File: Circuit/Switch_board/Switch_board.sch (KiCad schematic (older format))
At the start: 17 parts, among them J1 switch_mode, J2 switch, P1 XT30, Q1 BSS138, Q2 BSS138, U1 DRV5023

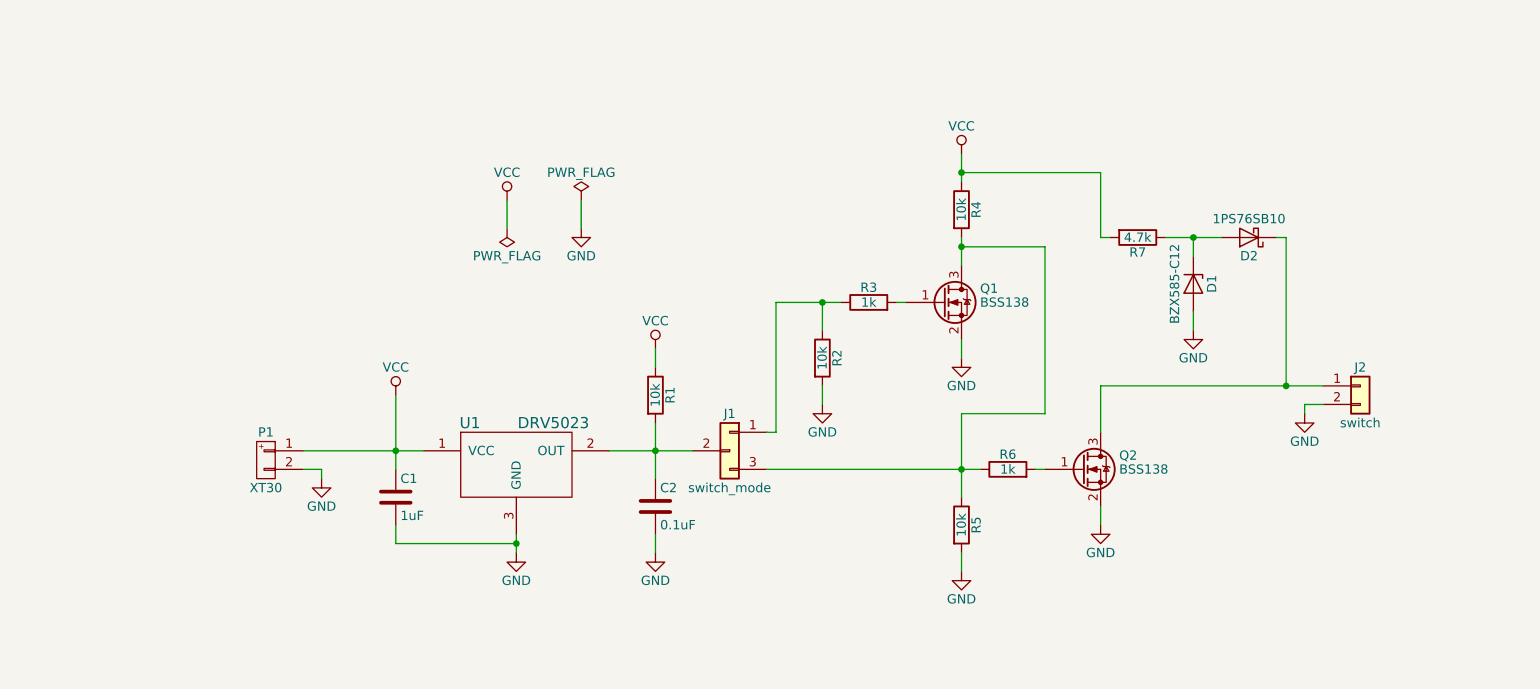
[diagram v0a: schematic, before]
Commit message: added status LED and change nMOSFET from BSS138 to 2N7002 in Switch_board
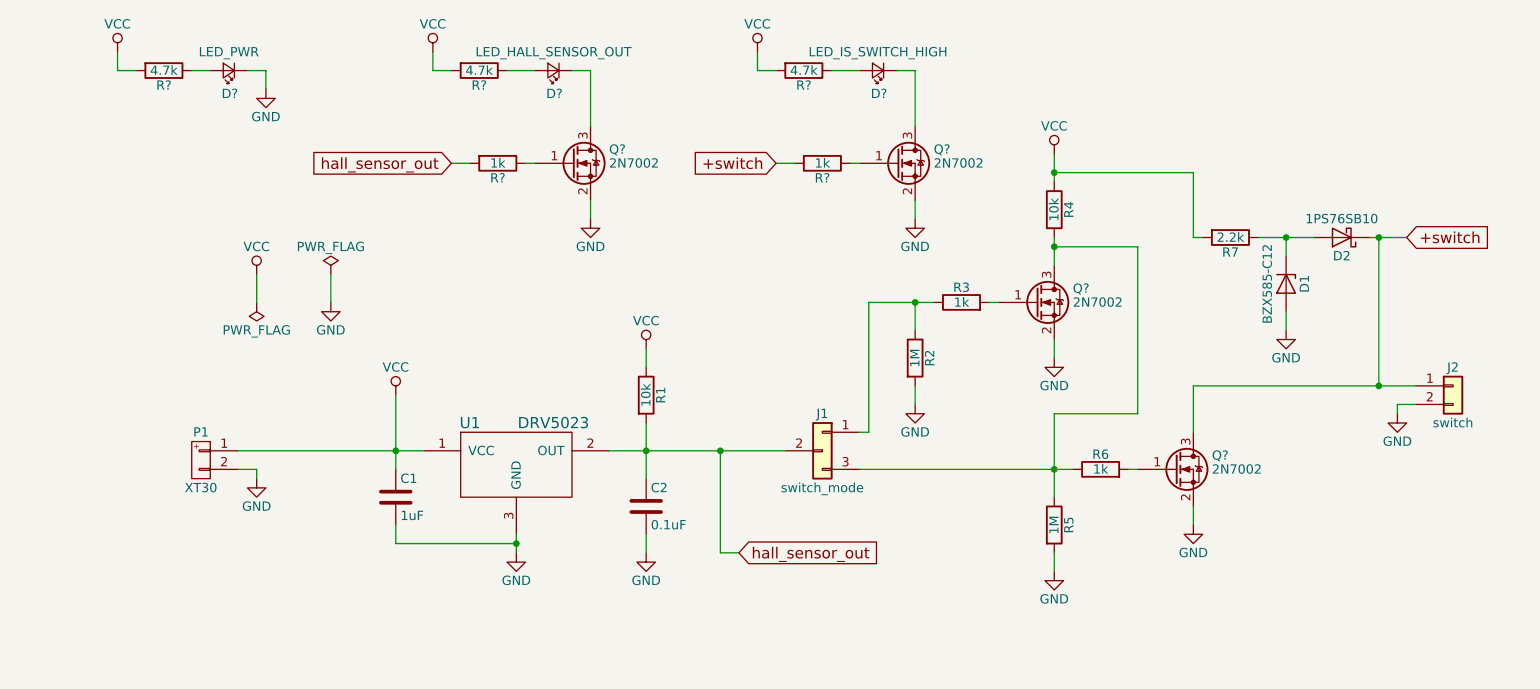
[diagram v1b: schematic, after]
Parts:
- removed Q1, Q2: BSS138, TO_SOT_Packages_SMD:SOT-23_Handsoldering, symbol BSS138
- added D?: LED_PWR, LEDs:LED_0603_HandSoldering, symbol LED_Small
- added D?: LED_HALL_SENSOR_OUT, LEDs:LED_0603_HandSoldering, symbol LED_Small
- added D?: LED_IS_SWITCH_HIGH, LEDs:LED_0603_HandSoldering, symbol LED_Small
- added Q? (x4): 2N7002, TO_SOT_Packages_SMD:SOT-23, symbol 2N7002
- added R? (x3): 4.7k, Resistors_SMD:R_0603_HandSoldering, symbol R
- added R? (x2): 1k, Resistors_SMD:R_0603_HandSoldering, symbol R
- R2, R5: value 10k -> 1M
- R7: value 4.7k -> 2.2k
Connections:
- net GND: now also D?.1 (K), Q?.2 (S), Q?.2 (S), Q?.2 (S), Q?.2 (S)
- net VCC: now also R?.2, R?.2, R?.2
- net hall_sensor_out: now reaches C2.1, J1.2 (Pin_2), R1.2, U1.2 (OUT)
- net hall_sensor_out: now also R?.2
- net at J1.3 (Pin_3), R4.2, R5.1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: now also Q?.3 (D)
- net +switch: now reaches D2.1 (K), J2.1 (Pin_1)
- net +switch: now also Q?.3 (D), R?.2
- net at R3.2: now also Q?.1 (G)
- net at R6.2: now also Q?.1 (G)
- new net: D?.2 (A), R?.1 (x3)
- new net: Q?.1 (G), R?.1 (x2)
- new net: D?.1 (K), Q?.3 (D) (x2)
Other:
- moved on the sheet: C2, D1, D2, J1, J2, P1, R1, R2, R3, R4, R5, R6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

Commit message: annoteted schematic and generated netlist of Switch_board
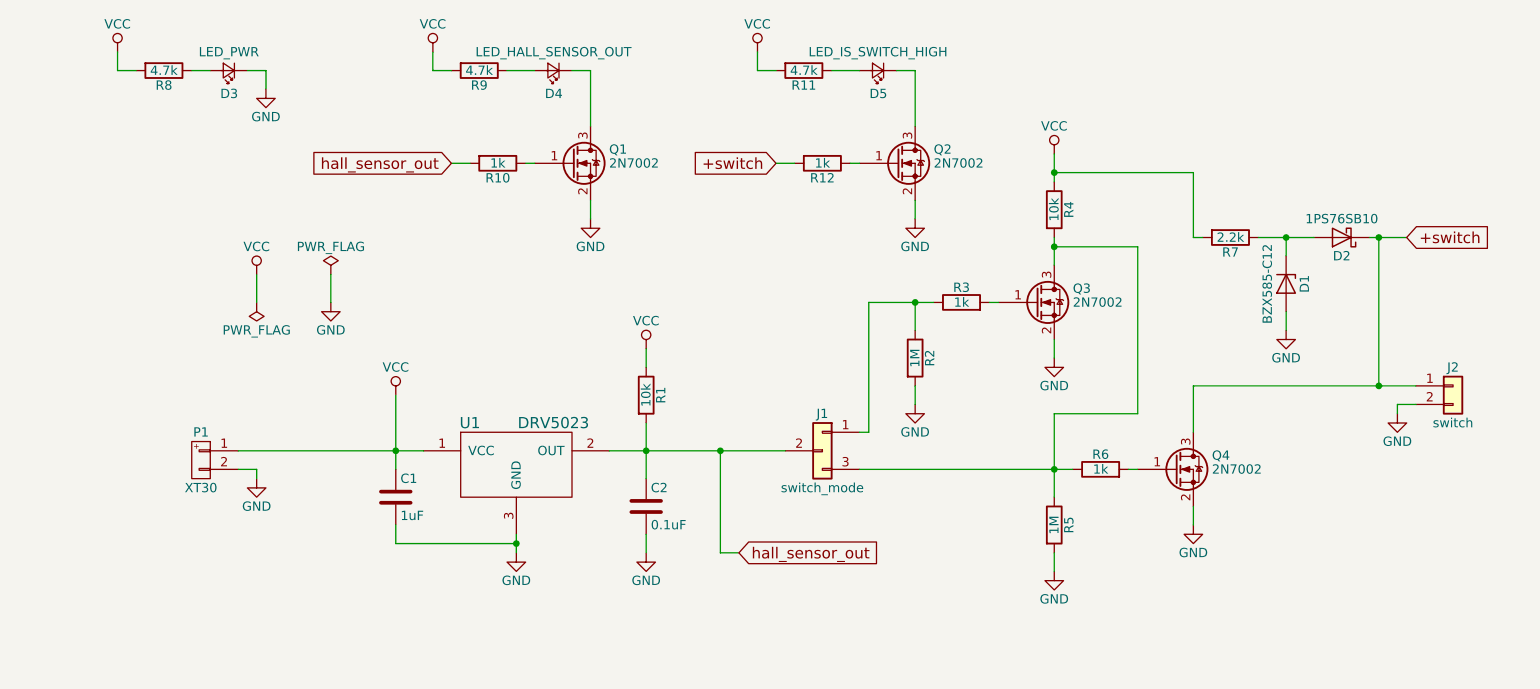
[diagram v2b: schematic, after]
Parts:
- gave numbers to parts that had none: 12
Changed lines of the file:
@@
 $EndComp
 $Comp
-L GND #PWR01
+L GND #PWR8
 U 1 1 5A826833
 P 3700 4750
-F 0 "#PWR01" H 3700 4500 50  0001 C CNN
+F 0 "#PWR8" H 3700 4500 50  0001 C CNN
 F 1 "GND" H 3700 4600 50  0000 C CNN
 F 2 "" H 3700 4750 50  0001 C CNN
@@
 $EndComp
 $Comp
-L GND #PWR02
+L GND #PWR3
 U 1 1 5A826918
 P 2300 4350
-F 0 "#PWR02" H 2300 4100 50  0001 C CNN
+F 0 "#PWR3" H 2300 4100 50  0001 C CNN
 F 1 "GND" H 2300 4200 50  0000 C CNN
 F 2 "" H 2300 4350 50  0001 C CNN
@@
 $EndComp
 $Comp
-L GND #PWR03
+L GND #PWR20
 U 1 1 5A829801
 P 8450 4000
-F 0 "#PWR03" H 8450 3750 50  0001 C CNN
+F 0 "#PWR20" H 8450 3750 50  0001 C CNN
 F 1 "GND" H 8450 3850 50  0000 C CNN
 F 2 "" H 8450 4000 50  0001 C CNN
@@
 $EndComp
 $Comp
-L GND #PWR04
+L GND #PWR14
 U 1 1 5A829CAE
 P 5850 3950
-F 0 "#PWR04" H 5850 3700 50  0001 C CNN
+F 0 "#PWR14" H 5850 3700 50  0001 C CNN
 F 1 "GND" H 5850 3800 50  0000 C CNN
 F 2 "" H 5850 3950 50  0001 C CNN
@@
 $EndComp
 $Comp
-L GND #PWR05
+L GND #PWR11
 U 1 1 5A883892
 P 4400 4750
-F 0 "#PWR05" H 4400 4500 50  0001 C CNN
+F 0 "#PWR11" H 4400 4500 50  0001 C CNN
 F 1 "GND" H 4400 4600 50  0000 C CNN
 F 2 "" H 4400 4750 50  0001 C CNN
@@
 $EndComp
 $Comp
-L GND #PWR06
+L GND #PWR16
 U 1 1 5A88921C
 P 6600 3700
-F 0 "#PWR06" H 6600 3450 50  0001 C CNN
+F 0 "#PWR16" H 6600 3450 50  0001 C CNN
 F 1 "GND" H 6600 3550 50  0000 C CNN
 F 2 "" H 6600 3700 50  0001 C CNN
@@
 $EndComp
 $Comp
-L VCC #PWR07
+L VCC #PWR6
 U 1 1 5A89DB47
 P 3050 3900
-F 0 "#PWR07" H 3050 3750 50  0001 C CNN
+F 0 "#PWR6" H 3050 3750 50  0001 C CNN
 F 1 "VCC" H 3050 4050 50  0000 C CNN
 F 2 "" H 3050 3900 50  0001 C CNN
@@
 $EndComp
 $Comp
-L GND #PWR08
+L GND #PWR19
 U 1 1 5A89F539
 P 7850 3550
-F 0 "#PWR08" H 7850 3300 50  0001 C CNN
+F 0 "#PWR19" H 7850 3300 50  0001 C CNN
 F 1 "GND" H 7850 3400 50  0000 C CNN
 F 2 "" H 7850 3550 50  0001 C CNN
@@
 $EndComp
 $Comp
-L GND #PWR09
+L GND #PWR17
 U 1 1 5A8DDCE5
 P 6600 4850
-F 0 "#PWR09" H 6600 4600 50  0001 C CNN
+F 0 "#PWR17" H 6600 4600 50  0001 C CNN
 F 1 "GND" H 6600 4700 50  0000 C CNN
 F 2 "" H 6600 4850 50  0001 C CNN
@@
 $EndComp
 $Comp
-L GND #PWR010
+L GND #PWR18
 U 1 1 5A8DDCF1
 P 7350 4600
-F 0 "#PWR010" H 7350 4350 50  0001 C CNN
+F 0 "#PWR18" H 7350 4350 50  0001 C CNN
 F 1 "GND" H 7350 4450 50  0000 C CNN
 F 2 "" H 7350 4600 50  0001 C CNN
@@
 $EndComp
 $Comp
-L VCC #PWR011
+L VCC #PWR15
 U 1 1 5A8DFBDA
 P 6600 2600
-F 0 "#PWR011" H 6600 2450 50  0001 C CNN
+F 0 "#PWR15" H 6600 2450 50  0001 C CNN
 F 1 "VCC" H 6600 2750 50  0000 C CNN
 F 2 "" H 6600 2600 50  0001 C CNN
@@
 $EndComp
 $Comp
-L VCC #PWR012
+L VCC #PWR10
 U 1 1 5A89E7B6
 P 4400 3650
-F 0 "#PWR012" H 4400 3500 50  0001 C CNN
+F 0 "#PWR10" H 4400 3500 50  0001 C CNN
 F 1 "VCC" H 4400 3800 50  0000 C CNN
 F 2 "" H 4400 3650 50  0001 C CNN
@@
 $EndComp
 $Comp
-L PWR_FLAG #FLG013
+L PWR_FLAG #FLG2
 U 1 1 5A8DF01C
 P 2700 3250
-F 0 "#FLG013" H 2700 3325 50  0001 C CNN
+F 0 "#FLG2" H 2700 3325 50  0001 C CNN
 F 1 "PWR_FLAG" H 2700 3400 50  0000 C CNN
 F 2 "" H 2700 3250 50  0001 C CNN
@@
 $EndComp
 $Comp
-L PWR_FLAG #FLG014
+L PWR_FLAG #FLG1
 U 1 1 5A8DF1C6
 P 2300 3400
-F 0 "#FLG014" H 2300 3475 50  0001 C CNN
+F 0 "#FLG1" H 2300 3475 50  0001 C CNN
 F 1 "PWR_FLAG" H 2300 3550 50  0000 C CNN
 F 2 "" H 2300 3400 50  0001 C CNN
@@
 $EndComp
 $Comp
-L VCC #PWR015
+L VCC #PWR2
 U 1 1 5A8E00E8
 P 2300 3250
-F 0 "#PWR015" H 2300 3100 50  0001 C CNN
+F 0 "#PWR2" H 2300 3100 50  0001 C CNN
 F 1 "VCC" H 2300 3400 50  0000 C CNN
 F 2 "" H 2300 3250 50  0001 C CNN
@@
 $EndComp
 $Comp
-L GND #PWR016
+L GND #PWR5
 U 1 1 5A8E04F5
 P 2700 3400
-F 0 "#PWR016" H 2700 3150 50  0001 C CNN
+F 0 "#PWR5" H 2700 3150 50  0001 C CNN
 F 1 "GND" H 2700 3250 50  0000 C CNN
 F 2 "" H 2700 3400 50  0001 C CNN
@@
 $EndComp
 $Comp
-L 2N7002 Q?
+L 2N7002 Q3
 U 1 1 5A90049A
 P 6500 3400
-F 0 "Q?" H 6700 3475 50  0000 L CNN
+F 0 "Q3" H 6700 3475 50  0000 L CNN
 F 1 "2N7002" H 6700 3400 50  0000 L CNN
 F 2 "TO_SOT_Packages_SMD:SOT-23" H 6700 3325 50  0001 L CIN
@@
 $EndComp
 $Comp
-L 2N7002 Q?
+L 2N7002 Q4
 U 1 1 5A900599
 P 7250 4300
-F 0 "Q?" H 7450 4375 50  0000 L CNN
+F 0 "Q4" H 7450 4375 50  0000 L CNN
 F 1 "2N7002" H 7450 4300 50  0000 L CNN
 F 2 "TO_SOT_Packages_SMD:SOT-23" H 7450 4225 50  0001 L CIN
@@
 $EndComp
 $Comp
-L VCC #PWR?
+L VCC #PWR1
 U 1 1 5A908EA5
 P 1550 2050
-F 0 "#PWR?" H 1550 1900 50  0001 C CNN
+F 0 "#PWR1" H 1550 1900 50  0001 C CNN
 F 1 "VCC" H 1550 2200 50  0000 C CNN
 F 2 "" H 1550 2050 50  0001 C CNN
@@
 $EndComp
 $Comp
-L R R?
+L R R8
 U 1 1 5A9099A7
 P 1800 2150
-F 0 "R?" V 1880 2150 50  0000 C CNN
+F 0 "R8" V 1880 2150 50  0000 C CNN
 F 1 "4.7k" V 1800 2150 50  0000 C CNN
 F 2 "Resistors_SMD:R_0603_HandSoldering" V 1730 2150 50  0001 C CNN
@@
 $EndComp
 $Comp
-L LED_Small D?
+L LED_Small D3
 U 1 1 5A909A38
 P 2150 2150
-F 0 "D?" H 2100 2275 50  0000 L CNN
+F 0 "D3" H 2100 2275 50  0000 L CNN
 F 1 "LED_PWR" H 2150 2050 50  0000 C CNN
 F 2 "LEDs:LED_0603_HandSoldering" V 2150 2150 50  0001 C CNN
@@
 $EndComp
 $Comp
-L GND #PWR?
+L GND #PWR4
 U 1 1 5A90AC6B
 P 2350 2250
-F 0 "#PWR?" H 2350 2000 50  0001 C CNN
+F 0 "#PWR4" H 2350 2000 50  0001 C CNN
 F 1 "GND" H 2350 2100 50  0000 C CNN
 F 2 "" H 2350 2250 50  0001 C CNN
@@
 $EndComp
 $Comp
-L 2N7002 Q?
+L 2N7002 Q1
 U 1 1 5A90F4A0
 P 4000 2650
-F 0 "Q?" H 4200 2725 50  0000 L CNN
+F 0 "Q1" H 4200 2725 50  0000 L CNN
 F 1 "2N7002" H 4200 2650 50  0000 L CNN
 F 2 "TO_SOT_Packages_SMD:SOT-23" H 4200 2575 50  0001 L CIN
@@
 $EndComp
 $Comp
-L R R?
+L R R10
 U 1 1 5A90F79A
 P 3600 2650
-F 0 "R?" V 3680 2650 50  0000 C CNN
+F 0 "R10" V 3680 2650 50  0000 C CNN
 F 1 "1k" V 3600 2650 50  0000 C CNN
 F 2 "Resistors_SMD:R_0603_HandSoldering" V 3530 2650 50  0001 C CNN
@@
 $EndComp
 $Comp
-L GND #PWR?
+L GND #PWR9
 U 1 1 5A90FC02
 P 4100 2950
-F 0 "#PWR?" H 4100 2700 50  0001 C CNN
+F 0 "#PWR9" H 4100 2700 50  0001 C CNN
 F 1 "GND" H 4100 2800 50  0000 C CNN
 F 2 "" H 4100 2950 50  0001 C CNN
@@
 $EndComp
 $Comp
-L R R?
+L R R9
 U 1 1 5A916BC0
 P 3500 2150
-F 0 "R?" V 3580 2150 50  0000 C CNN
+F 0 "R9" V 3580 2150 50  0000 C CNN
 F 1 "4.7k" V 3500 2150 50  0000 C CNN
 F 2 "Resistors_SMD:R_0603_HandSoldering" V 3430 2150 50  0001 C CNN
@@
 $EndComp
 $Comp
-L LED_Small D?
+L LED_Small D4
 U 1 1 5A916BC6
 P 3900 2150
-F 0 "D?" H 3850 2275 50  0000 L CNN
+F 0 "D4" H 3850 2275 50  0000 L CNN
 F 1 "LED_HALL_SENSOR_OUT" H 3900 2050 50  0000 C CNN
 F 2 "LEDs:LED_0603_HandSoldering" V 3900 2150 50  0001 C CNN
@@
 $EndComp
 $Comp
-L VCC #PWR?
+L VCC #PWR7
 U 1 1 5A919C90
 P 3250 2050
-F 0 "#PWR?" H 3250 1900 50  0001 C CNN
+F 0 "#PWR7" H 3250 1900 50  0001 C CNN
 F 1 "VCC" H 3250 2200 50  0000 C CNN
 F 2 "" H 3250 2050 50  0001 C CNN
@@
 	4100 2150 4100 2450
 $Comp
-L 2N7002 Q?
+L 2N7002 Q2
 U 1 1 5A932A55
 P 5750 2650
-F 0 "Q?" H 5950 2725 50  0000 L CNN
+F 0 "Q2" H 5950 2725 50  0000 L CNN
 F 1 "2N7002" H 5950 2650 50  0000 L CNN
 F 2 "TO_SOT_Packages_SMD:SOT-23" H 5950 2575 50  0001 L CIN
@@
 $EndComp
 $Comp
-L R R?
+L R R12
 U 1 1 5A932A5B
 P 5350 2650
-F 0 "R?" V 5430 2650 50  0000 C CNN
+F 0 "R12" V 5430 2650 50  0000 C CNN
 F 1 "1k" V 5350 2650 50  0000 C CNN
 F 2 "Resistors_SMD:R_0603_HandSoldering" V 5280 2650 50  0001 C CNN
@@
 $EndComp
 $Comp
-L GND #PWR?
+L GND #PWR13
 U 1 1 5A932A61
 P 5850 2950
-F 0 "#PWR?" H 5850 2700 50  0001 C CNN
+F 0 "#PWR13" H 5850 2700 50  0001 C CNN
 F 1 "GND" H 5850 2800 50  0000 C CNN
 F 2 "" H 5850 2950 50  0001 C CNN
@@
 $EndComp
 $Comp
-L R R?
+L R R11
 U 1 1 5A932A67
 P 5250 2150
-F 0 "R?" V 5330 2150 50  0000 C CNN
+F 0 "R11" V 5330 2150 50  0000 C CNN
 F 1 "4.7k" V 5250 2150 50  0000 C CNN
 F 2 "Resistors_SMD:R_0603_HandSoldering" V 5180 2150 50  0001 C CNN
@@
 $EndComp
 $Comp
-L LED_Small D?
+L LED_Small D5
 U 1 1 5A932A6D
 P 5650 2150
-F 0 "D?" H 5600 2275 50  0000 L CNN
+F 0 "D5" H 5600 2275 50  0000 L CNN
 F 1 "LED_IS_SWITCH_HIGH" H 5650 2050 50  0000 C CNN
 F 2 "LEDs:LED_0603_HandSoldering" V 5650 2150 50  0001 C CNN
@@
 $EndComp
 $Comp
-L VCC #PWR?
+L VCC #PWR12
 U 1 1 5A932A73
 P 5000 2050
-F 0 "#PWR?" H 5000 1900 50  0001 C CNN
+F 0 "#PWR12" H 5000 1900 50  0001 C CNN
 F 1 "VCC" H 5000 2200 50  0000 C CNN
 F 2 "" H 5000 2050 50  0001 C CNN

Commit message: changed SOT-23 footprints on Switch_board to SOT-23_handsoldering footprints
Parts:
- Q1, Q2, Q3, Q4: footprint TO_SOT_Packages_SMD:SOT-23 -> TO_SOT_Packages_SMD:SOT-23_Handsoldering
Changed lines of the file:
@@
 F 0 "Q3" H 6700 3475 50  0000 L CNN
 F 1 "2N7002" H 6700 3400 50  0000 L CNN
-F 2 "TO_SOT_Packages_SMD:SOT-23" H 6700 3325 50  0001 L CIN
+F 2 "TO_SOT_Packages_SMD:SOT-23_Handsoldering" H 6700 3325 50  0001 L CIN
 F 3 "" H 6500 3400 50  0001 L CNN
 	1    6500 3400
@@
 F 0 "Q4" H 7450 4375 50  0000 L CNN
 F 1 "2N7002" H 7450 4300 50  0000 L CNN
-F 2 "TO_SOT_Packages_SMD:SOT-23" H 7450 4225 50  0001 L CIN
+F 2 "TO_SOT_Packages_SMD:SOT-23_Handsoldering" H 7450 4225 50  0001 L CIN
 F 3 "" H 7250 4300 50  0001 L CNN
 	1    7250 4300
@@
 F 0 "Q1" H 4200 2725 50  0000 L CNN
 F 1 "2N7002" H 4200 2650 50  0000 L CNN
-F 2 "TO_SOT_Packages_SMD:SOT-23" H 4200 2575 50  0001 L CIN
+F 2 "TO_SOT_Packages_SMD:SOT-23_Handsoldering" H 4200 2575 50  0001 L CIN
 F 3 "" H 4000 2650 50  0001 L CNN
 	1    4000 2650
@@
 F 0 "Q2" H 5950 2725 50  0000 L CNN
 F 1 "2N7002" H 5950 2650 50  0000 L CNN
-F 2 "TO_SOT_Packages_SMD:SOT-23" H 5950 2575 50  0001 L CIN
+F 2 "TO_SOT_Packages_SMD:SOT-23_Handsoldering" H 5950 2575 50  0001 L CIN
 F 3 "" H 5750 2650 50  0001 L CNN
 	1    5750 2650

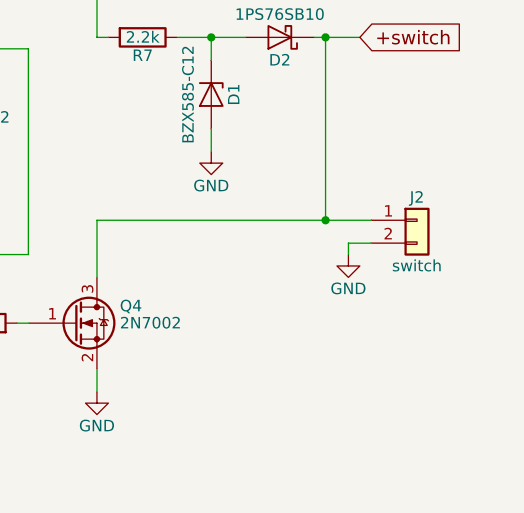
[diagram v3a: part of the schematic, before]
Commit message: added silkskin for connectors on Switch_board
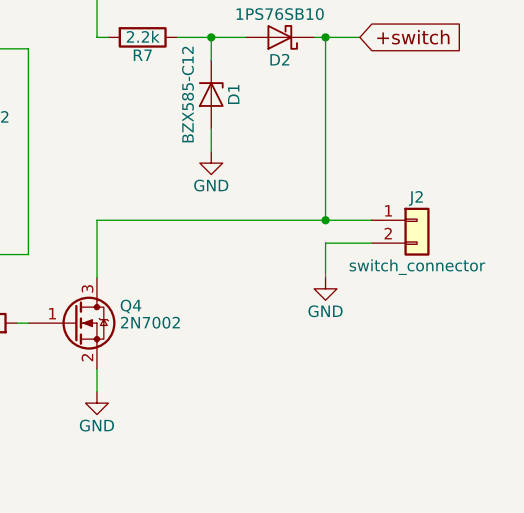
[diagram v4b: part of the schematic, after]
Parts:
- J2: value switch -> switch_connector
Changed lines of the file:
@@
 P 8750 3850
 F 0 "J2" H 8750 3950 50  0000 C CNN
-F 1 "switch" H 8750 3650 50  0000 C CNN
+F 1 "switch_connector" H 8750 3650 50  0000 C CNN
 F 2 "zeabus:90136-1202" H 8750 3850 50  0001 C CNN
 F 3 "" H 8750 3850 50  0001 C CNN
@@
 L GND #PWR20
 U 1 1 5A829801
-P 8450 4000
-F 0 "#PWR20" H 8450 3750 50  0001 C CNN
-F 1 "GND" H 8450 3850 50  0000 C CNN
-F 2 "" H 8450 4000 50  0001 C CNN
-F 3 "" H 8450 4000 50  0001 C CNN
-	1    8450 4000
+P 8350 4100
+F 0 "#PWR20" H 8350 3850 50  0001 C CNN
+F 1 "GND" H 8350 3950 50  0000 C CNN
+F 2 "" H 8350 4100 50  0001 C CNN
+F 3 "" H 8350 4100 50  0001 C CNN
+	1    8350 4100
 	1    0    0    -1
 $EndComp
@@
 Connection ~ 4400 4200
 Wire Wire Line
-	8550 3950 8450 3950
+	8350 3950 8550 3950
 Wire Wire Line
 	2300 4300 2300 4350
-Wire Wire Line
-	8450 3950 8450 4000
 Wire Wire Line
 	4400 3650 4400 3750
@@
 Wire Wire Line
 	5850 2150 5850 2450
+Wire Wire Line
+	8350 3950 8350 4100
 $EndSCHEMATC

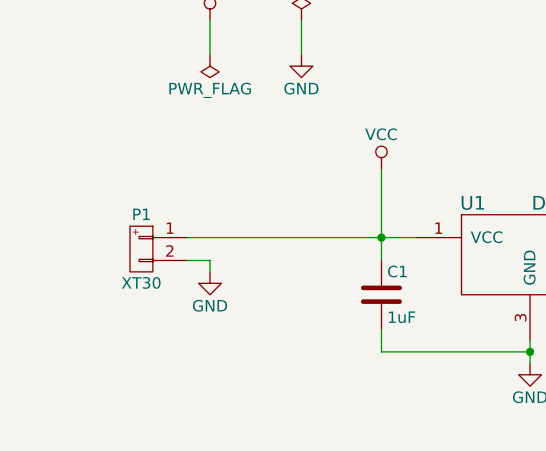
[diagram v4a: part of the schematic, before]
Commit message: changed 'SW CONN' to 'SW_CONN' and added SW_MODE silkskins on PCB of Switch_board
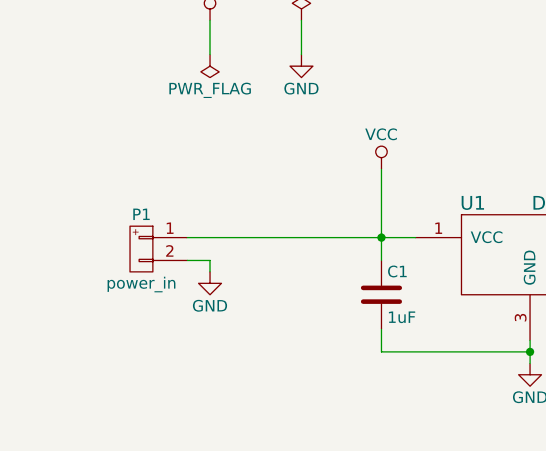
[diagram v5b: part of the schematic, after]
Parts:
- P1: value XT30 -> power_in
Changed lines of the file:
@@
 P 2000 4250
 F 0 "P1" H 2000 4400 50  0000 C CNN
-F 1 "XT30" H 2000 4100 50  0000 C CNN
+F 1 "power_in" H 2000 4100 50  0000 C CNN
 F 2 "zeabus:XT30" H 2000 4250 60  0001 C CNN
 F 3 "" H 2000 4250 60  0000 C CNN
